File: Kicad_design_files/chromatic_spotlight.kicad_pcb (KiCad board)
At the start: 2 copper layers, 45.7 x 73.7 mm, 36 parts, among them CON1 POWER_CONN, P1 CONN_6, Q1 MOSFET_N, Q2 MOSFET_N, SW1 SLIDE 1PDT, U1 LT3474, U2 LT3474

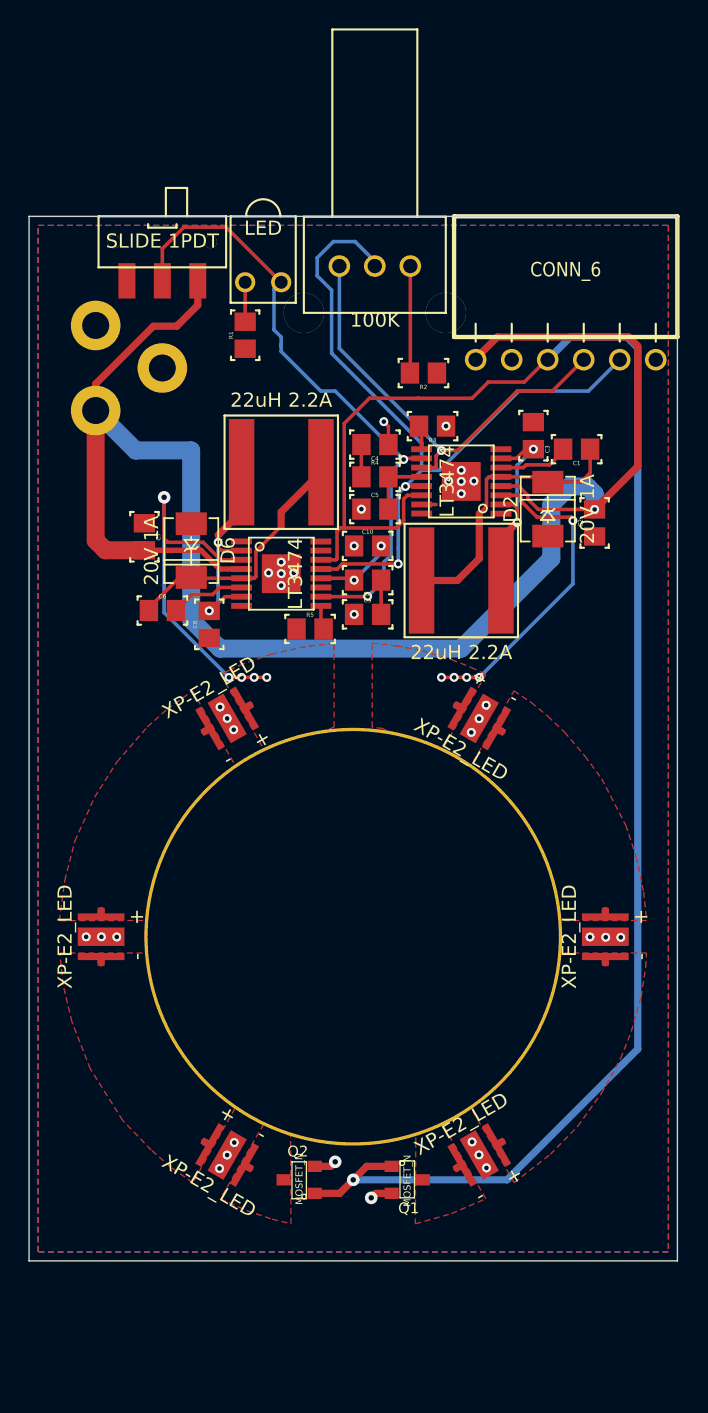
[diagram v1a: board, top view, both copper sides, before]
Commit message: reviewed, added screw holes
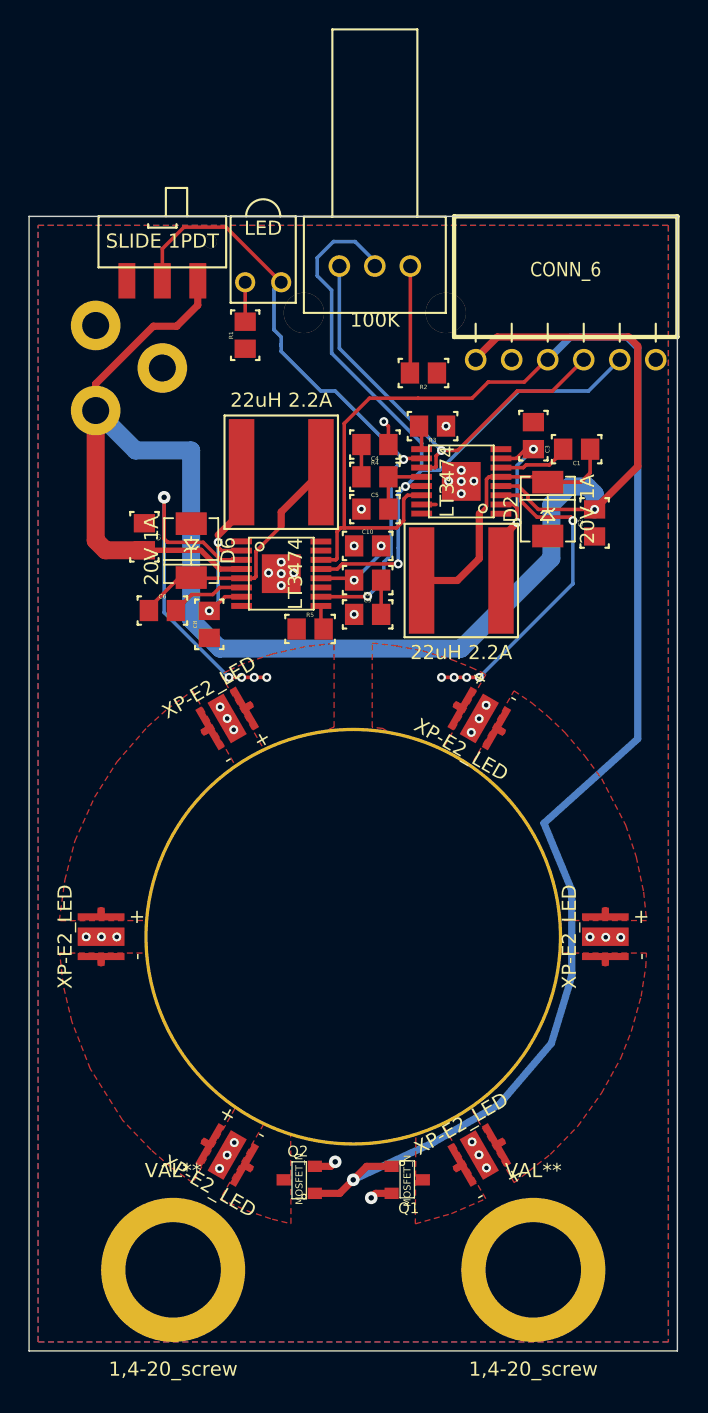
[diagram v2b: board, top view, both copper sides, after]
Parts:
- added 1,4-20_screw: VAL**, 1,4-20_screw, F.Cu at (-12.7, 23.5)
- added 1,4-20_screw: VAL**, 1,4-20_screw, F.Cu at (12.7, 23.5)
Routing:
- net /LED_ARRAY_1/TRIGGER: track 121.4 -> 118.0 mm
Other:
- board size 45.7 x 73.7 mm -> 45.7 x 80 mm
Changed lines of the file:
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@@
 (kicad_pcb (version 3) (host pcbnew "(2013-07-07 BZR 4022)-stable")
   (general
-    (links 94)
+    (links 96)
     (no_connects 0)
     (area -24.440444 -64.210001 23.164801 22.910001)
     (thickness 1.6)
     (drawings 4)
-    (tracks 286)
+    (tracks 294)
     (zones 0)
-    (modules 36)
+    (modules 38)
     (nets 29)
   )
@@
   )
   (layers
-    (15 F.Cu signal hide)
-    (0 B.Cu signal)
+    (15 F.Cu signal)
+    (0 B.Cu signal hide)
     (16 B.Adhes user hide)
     (17 F.Adhes user hide)
@@
   )
   (setup
-    (last_trace_width 0.254)
+    (last_trace_width 0.508)
     (user_trace_width 0.254)
     (user_trace_width 0.381)
@@
     (mod_text_size 1 1)
     (mod_text_width 0.15)
-    (pad_size 29.464 29.464)
-    (pad_drill 29)
+    (pad_size 10.16 10.16)
+    (pad_drill 6.731)
     (pad_to_mask_clearance 0)
     (aux_axis_origin 0 0)
@@
     )
   )
-  (gr_line (start -22.86 -50.8) (end -22.86 22.86) (angle 90) (layer Edge.Cuts) (width 0.1))
+  (module 1,4-20_screw (layer F.Cu)
+    (at -12.7 23.495)
+    (fp_text reference 1,4-20_screw (at 0 7) (layer F.SilkS)
+      (effects (font (size 1 1) (thickness 0.15)))
+    )
+    (fp_text value VAL** (at 0 -7) (layer F.SilkS)
+      (effects (font (size 1 1) (thickness 0.15)))
+    )
+    (pad 1 thru_hole circle (at 0 0) (size 10.16 10.16) (drill 6.731)
+      (layers *.Cu *.Mask F.SilkS)
+      (net 14 GND)
+      (zone_connect 2)
+    )
+  )
+  (module 1,4-20_screw (layer F.Cu)
+    (at 12.7 23.495)
+    (fp_text reference 1,4-20_screw (at 0 7) (layer F.SilkS)
+      (effects (font (size 1 1) (thickness 0.15)))
+    )
+    (fp_text value VAL** (at 0 -7) (layer F.SilkS)
+      (effects (font (size 1 1) (thickness 0.15)))
+    )
+    (pad 1 thru_hole circle (at 0 0) (size 10.16 10.16) (drill 6.731)
+      (layers *.Cu *.Mask F.SilkS)
+      (net 14 GND)
+      (zone_connect 2)
+    )
+  )
+  (gr_line (start -22.86 -50.8) (end -22.86 29.21) (angle 90) (layer Edge.Cuts) (width 0.1))
   (gr_line (start 22.86 -50.8) (end -22.86 -50.8) (angle 90) (layer Edge.Cuts) (width 0.1))
-  (gr_line (start 22.86 22.86) (end 22.86 -50.8) (angle 90) (layer Edge.Cuts) (width 0.1))
-  (gr_line (start -22.86 22.86) (end 22.86 22.86) (angle 90) (layer Edge.Cuts) (width 0.1))
+  (gr_line (start 22.86 29.21) (end 22.86 -50.8) (angle 90) (layer Edge.Cuts) (width 0.1))
+  (gr_line (start -22.86 29.21) (end 22.86 29.21) (angle 90) (layer Edge.Cuts) (width 0.1))
   (segment (start 8.636 -40.6908) (end 8.636 -40.767) (width 0.508) (layer F.Cu) (net 1))
   (segment (start 20.066 -33.17494) (end 17.02308 -30.13202) (width 0.508) (layer F.Cu) (net 1))
@@
   (segment (start -11.938 -50.038) (end -8.9662 -50.038) (width 0.254) (layer F.Cu) (net 3))
   (segment (start -13.462 -48.514) (end -11.938 -50.038) (width 0.254) (layer F.Cu) (net 3))
-  (segment (start 13.716 -40.6908) (end 15.3162 -42.291) (width 0.508) (layer B.Cu) (net 4))
+  (segment (start 15.412946 -3.260956) (end 13.4493 -8.001) (width 0.508) (layer B.Cu) (net 4))
+  (segment (start 15.3162 -42.291) (end 19.304 -42.291) (width 0.508) (layer B.Cu) (net 4))
+  (segment (start 19.304 -42.291) (end 20.066 -41.529) (width 0.508) (layer B.Cu) (net 4))
+  (segment (start 15.3162 -42.291) (end 13.716 -40.6908) (width 0.508) (layer B.Cu) (net 4))
+  (segment (start 20.066 -13.95476) (end 20.066 -41.529) (width 0.508) (layer B.Cu) (net 4))
+  (segment (start 13.4493 -8.001) (end 20.066 -13.95476) (width 0.508) (layer B.Cu) (net 4))
+  (segment (start 0 17.145) (end 5.59308 14.54404) (width 0.508) (layer B.Cu) (net 4))
   (via (at 0 17.145) (size 0.889) (layers F.Cu B.Cu) (net 4))
-  (segment (start 10.84834 17.145) (end 0 17.145) (width 0.508) (layer B.Cu) (net 4))
-  (segment (start 20.066 7.92734) (end 10.84834 17.145) (width 0.508) (layer B.Cu) (net 4))
-  (segment (start 20.066 -41.529) (end 20.066 7.92734) (width 0.508) (layer B.Cu) (net 4))
-  (segment (start 19.304 -42.291) (end 20.066 -41.529) (width 0.508) (layer B.Cu) (net 4))
-  (segment (start 15.3162 -42.291) (end 19.304 -42.291) (width 0.508) (layer B.Cu) (net 4))
+  (segment (start 15.41526 -2.58064) (end 15.412946 -3.260956) (width 0.508) (layer B.Cu) (net 4))
+  (segment (start 15.412946 -3.260956) (end 15.41272 -3.3274) (width 0.508) (layer B.Cu) (net 4))
+  (segment (start 15.41526 2.68478) (end 15.41526 -2.58064) (width 0.508) (layer B.Cu) (net 4))
+  (segment (start 15.21968 3.43154) (end 15.41526 2.68478) (width 0.508) (layer B.Cu) (net 4))
+  (segment (start 13.97508 7.52094) (end 15.21968 3.43154) (width 0.508) (layer B.Cu) (net 4))
+  (segment (start 10.287 11.84148) (end 13.97508 7.52094) (width 0.508) (layer B.Cu) (net 4))
+  (segment (start 5.59308 14.54404) (end 10.287 11.84148) (width 0.508) (layer B.Cu) (net 4))
   (segment (start 4.572 -37.973) (end 1.143 -37.973) (width 0.254) (layer F.Cu) (net 4))
   (segment (start 13.6398 -40.6908) (end 12.065 -39.116) (width 0.254) (layer F.Cu) (net 4))
@@
     (polygon
       (pts
-        (xy 22.225 22.225) (xy -22.225 22.225) (xy -22.225 -50.165) (xy 22.225 -50.165)
+        (xy 22.225 28.575) (xy -22.225 28.575) (xy -22.225 -50.165) (xy 22.225 -50.165)
       )
     )
@@
     (polygon
       (pts
-        (xy 22.225 22.225) (xy -22.225 22.225) (xy -22.225 -50.165) (xy 22.225 -50.165)
+        (xy 22.225 28.575) (xy -22.225 28.575) (xy -22.225 -50.165) (xy 22.225 -50.165)
       )
     )

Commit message: going to try to reset global texts
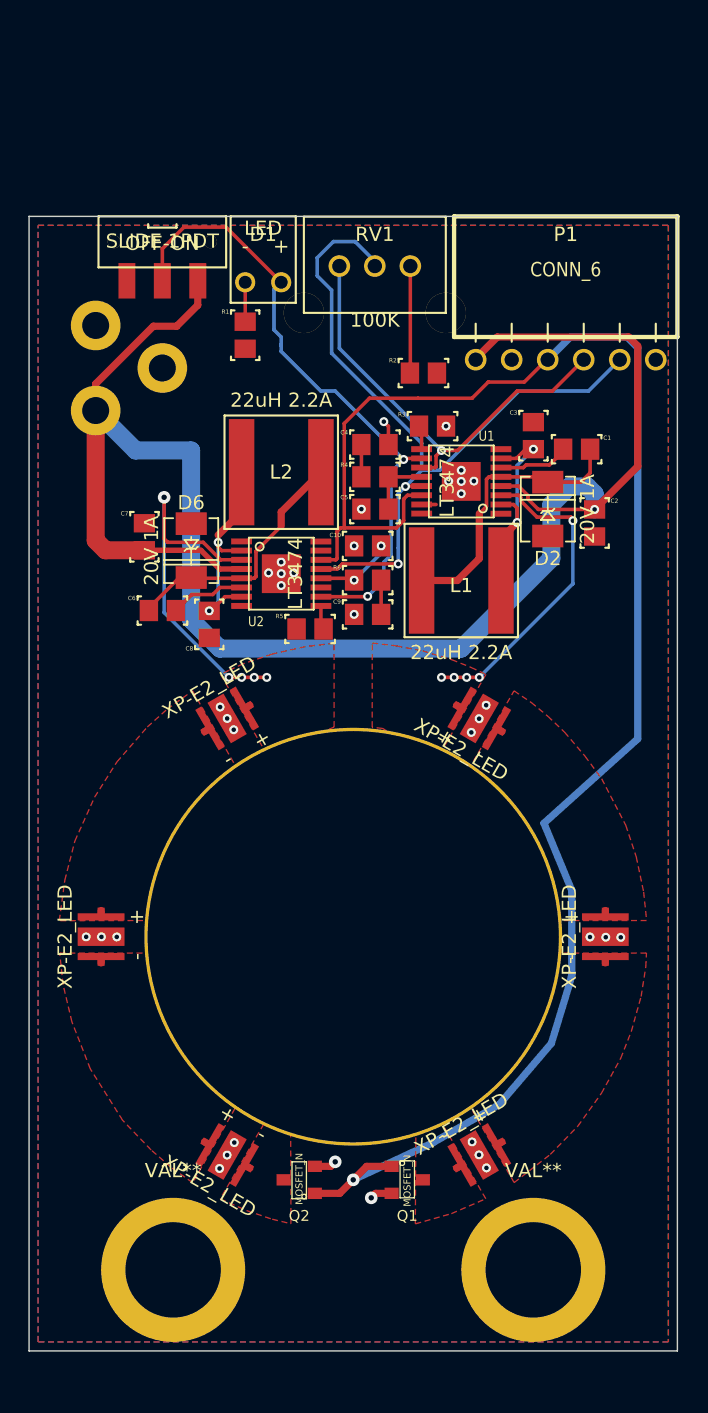
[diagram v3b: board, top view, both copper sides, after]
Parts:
- renumbered SW1 to OFF-ON
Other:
- rule pad_to_mask_clearance: 0 -> 0.1778

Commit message: added manufacturing files
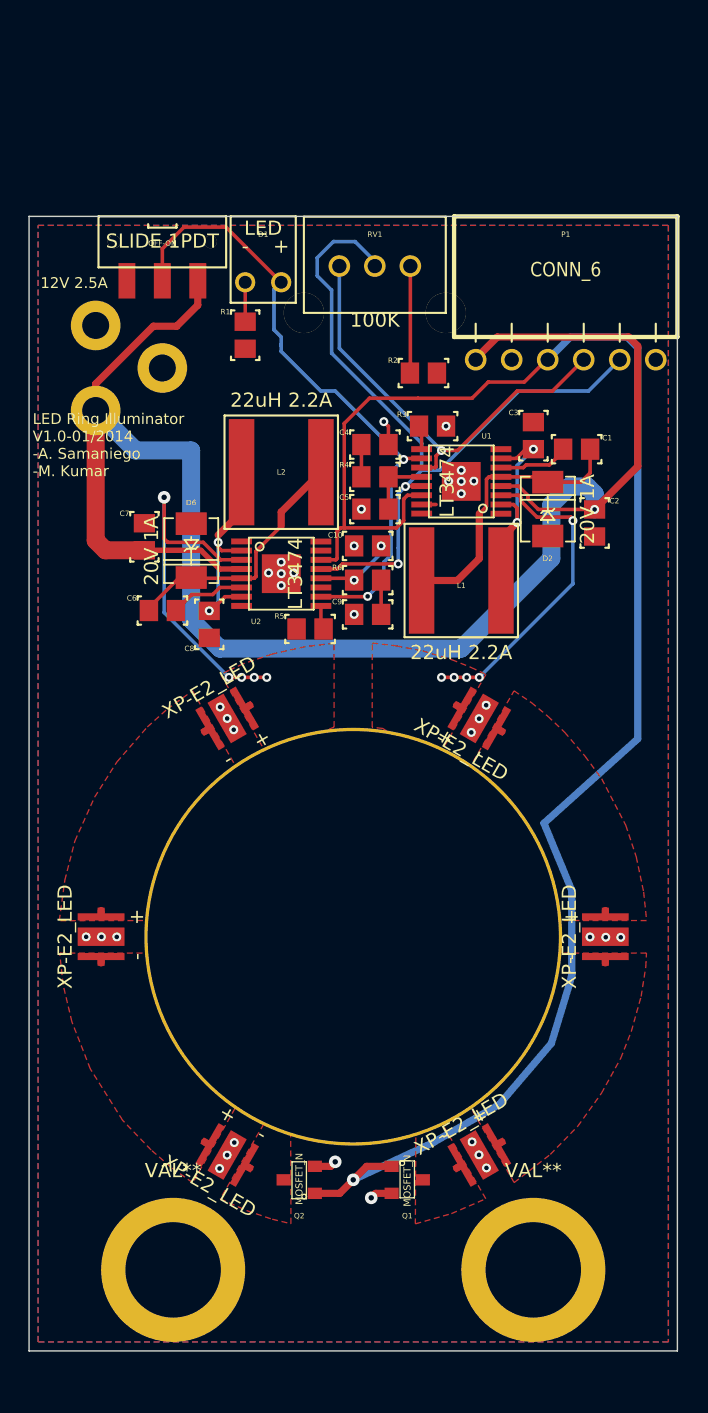
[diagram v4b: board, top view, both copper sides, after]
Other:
- board text added: "12V 2.5A"
- board text added: "LED Ring Illuminator V1.0-01/2014 -A. Samaniego -M. Kumar"
